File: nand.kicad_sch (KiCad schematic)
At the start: 20 parts, among them U6 IS21ES08GA-JQLI-TR

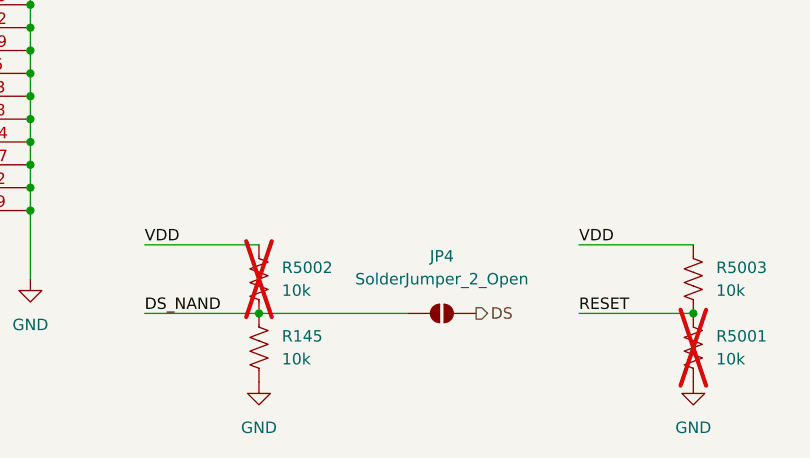
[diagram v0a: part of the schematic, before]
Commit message: eMMC routing
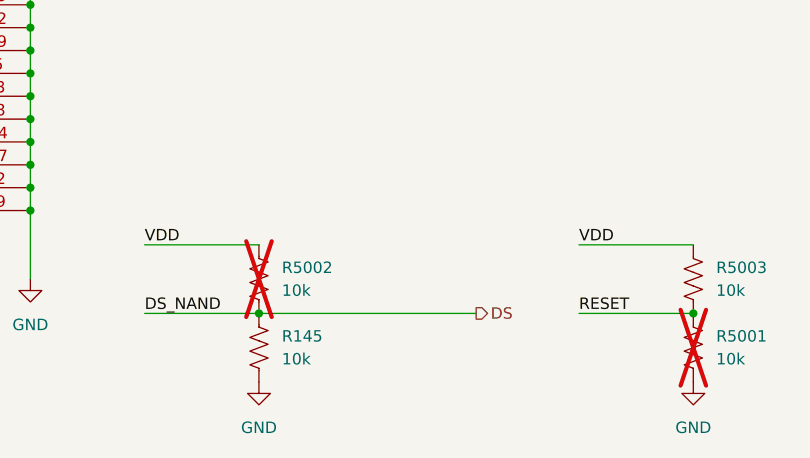
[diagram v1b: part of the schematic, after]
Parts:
- removed JP4: SolderJumper_2_Open, Jumper:SolderJumper-2_P1.3mm_Open_Pad1.0x1.5mm, symbol Jumper:SolderJumper_2_Open
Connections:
- net DS_NAND is gone; now on net DS: R145.1, R5002.2, U6.K5 (DS)
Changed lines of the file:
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@@
 	(wire
 		(pts
-			(xy 109.22 176.53) (xy 125.73 176.53)
+			(xy 109.22 176.53) (xy 133.35 176.53)
 		)
 		(stroke
@@
 					(unit 1)
 				)
-			)
-		)
-	)
-	(symbol
-		(lib_name "SolderJumper_2_Open_1")
-		(lib_id "Jumper:SolderJumper_2_Open")
-		(at 129.54 176.53 0)
-		(unit 1)
-		(exclude_from_sim no)
-		(in_bom no)
-		(on_board yes)
-		(dnp no)
-		(fields_autoplaced yes)
-		(property "Reference" "JP4"
-			(at 129.54 170.18 0)
-			(effects
-				(font
-					(size 1.27 1.27)
-				)
-			)
-		)
-		(property "Value" "SolderJumper_2_Open"
-			(at 129.54 172.72 0)
-			(effects
-				(font
-					(size 1.27 1.27)
-				)
-			)
-		)
-		(property "Footprint" "Jumper:SolderJumper-2_P1.3mm_Open_Pad1.0x1.5mm"
-			(at 129.54 176.53 0)
-			(effects
-				(font
-					(size 1.27 1.27)
-				)
-				(hide yes)
-			)
-		)
-		(property "Datasheet" "~"
-			(at 129.54 176.53 0)
-			(effects
-				(font
-					(size 1.27 1.27)
-				)
-				(hide yes)
-			)
-		)
-		(property "Description" "Solder Jumper, 2-pole, open"
-			(at 129.54 176.53 0)
-			(effects
-				(font
-					(size 1.27 1.27)
-				)
-				(hide yes)
-			)
-		)
-		(pin "2"
-		)
-		(pin "1"
-		)
-		(instances
-			(project ""
-				(path "/21bb932a-ec67-4661-9215-0551f718d1c0/dbc4538f-6782-4334-8773-c54462e4bd8b"
-					(reference "JP4")
-					(unit 1)
-				)

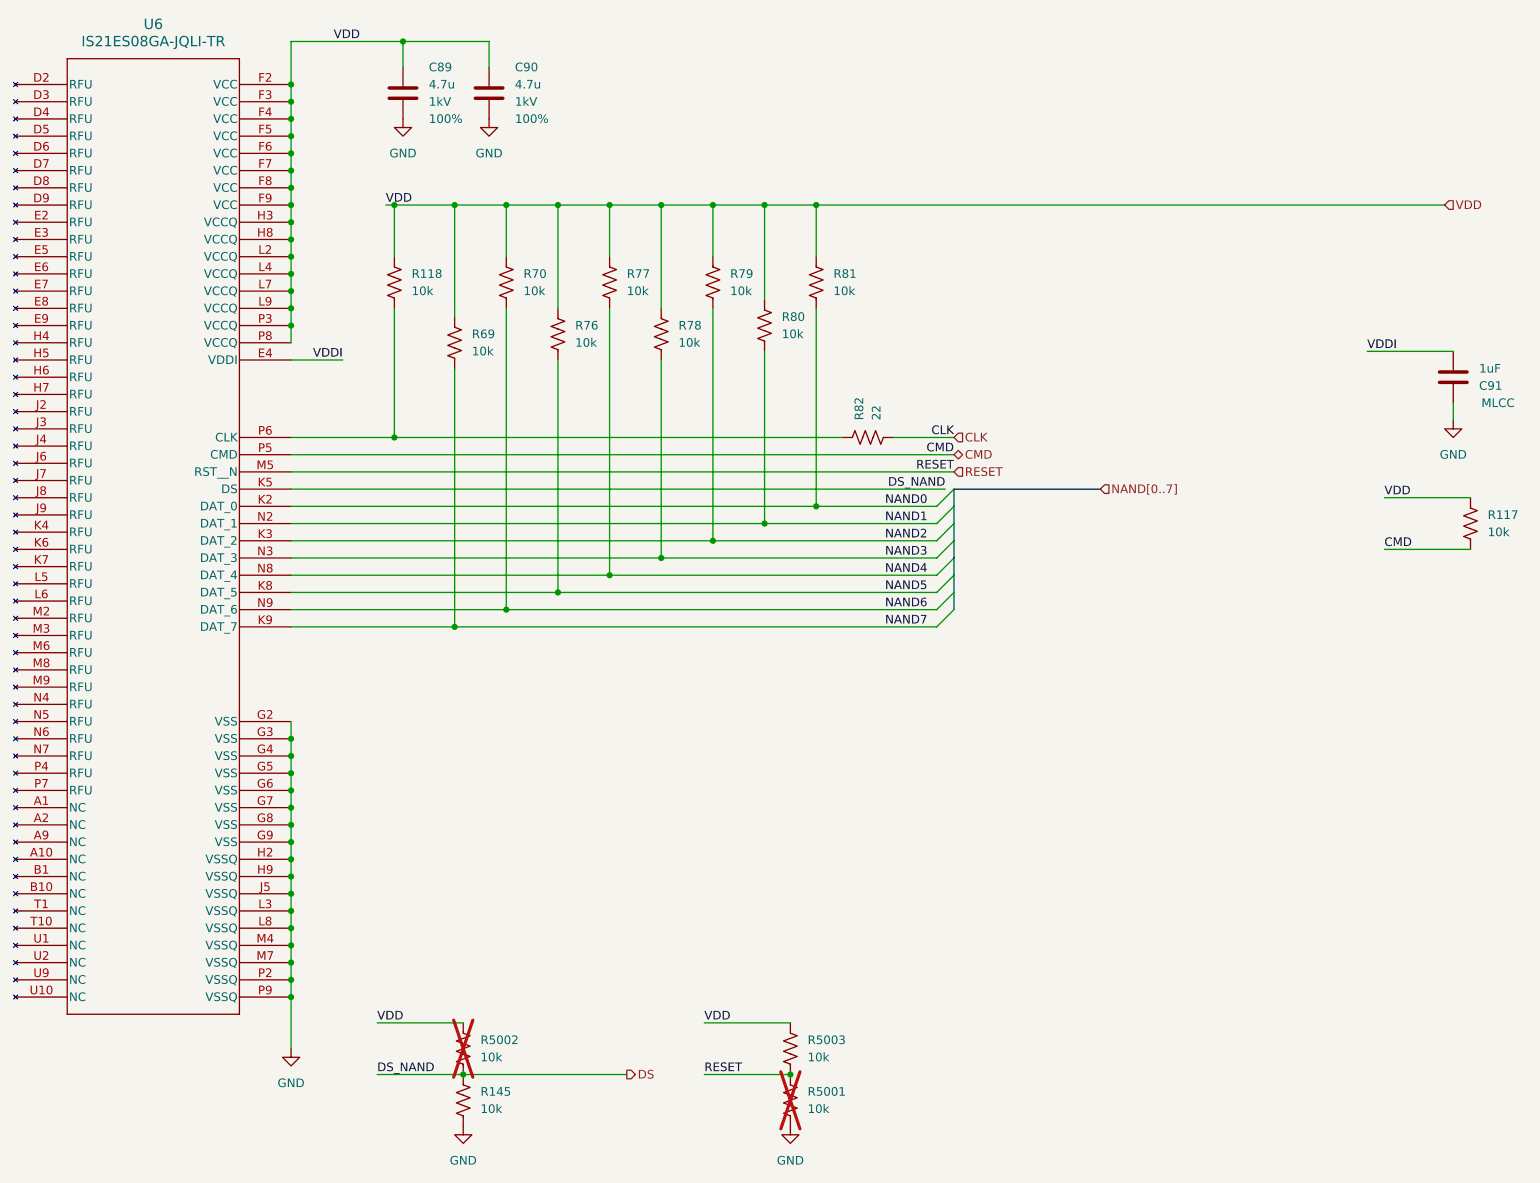
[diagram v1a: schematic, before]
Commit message: Organizing REFDES
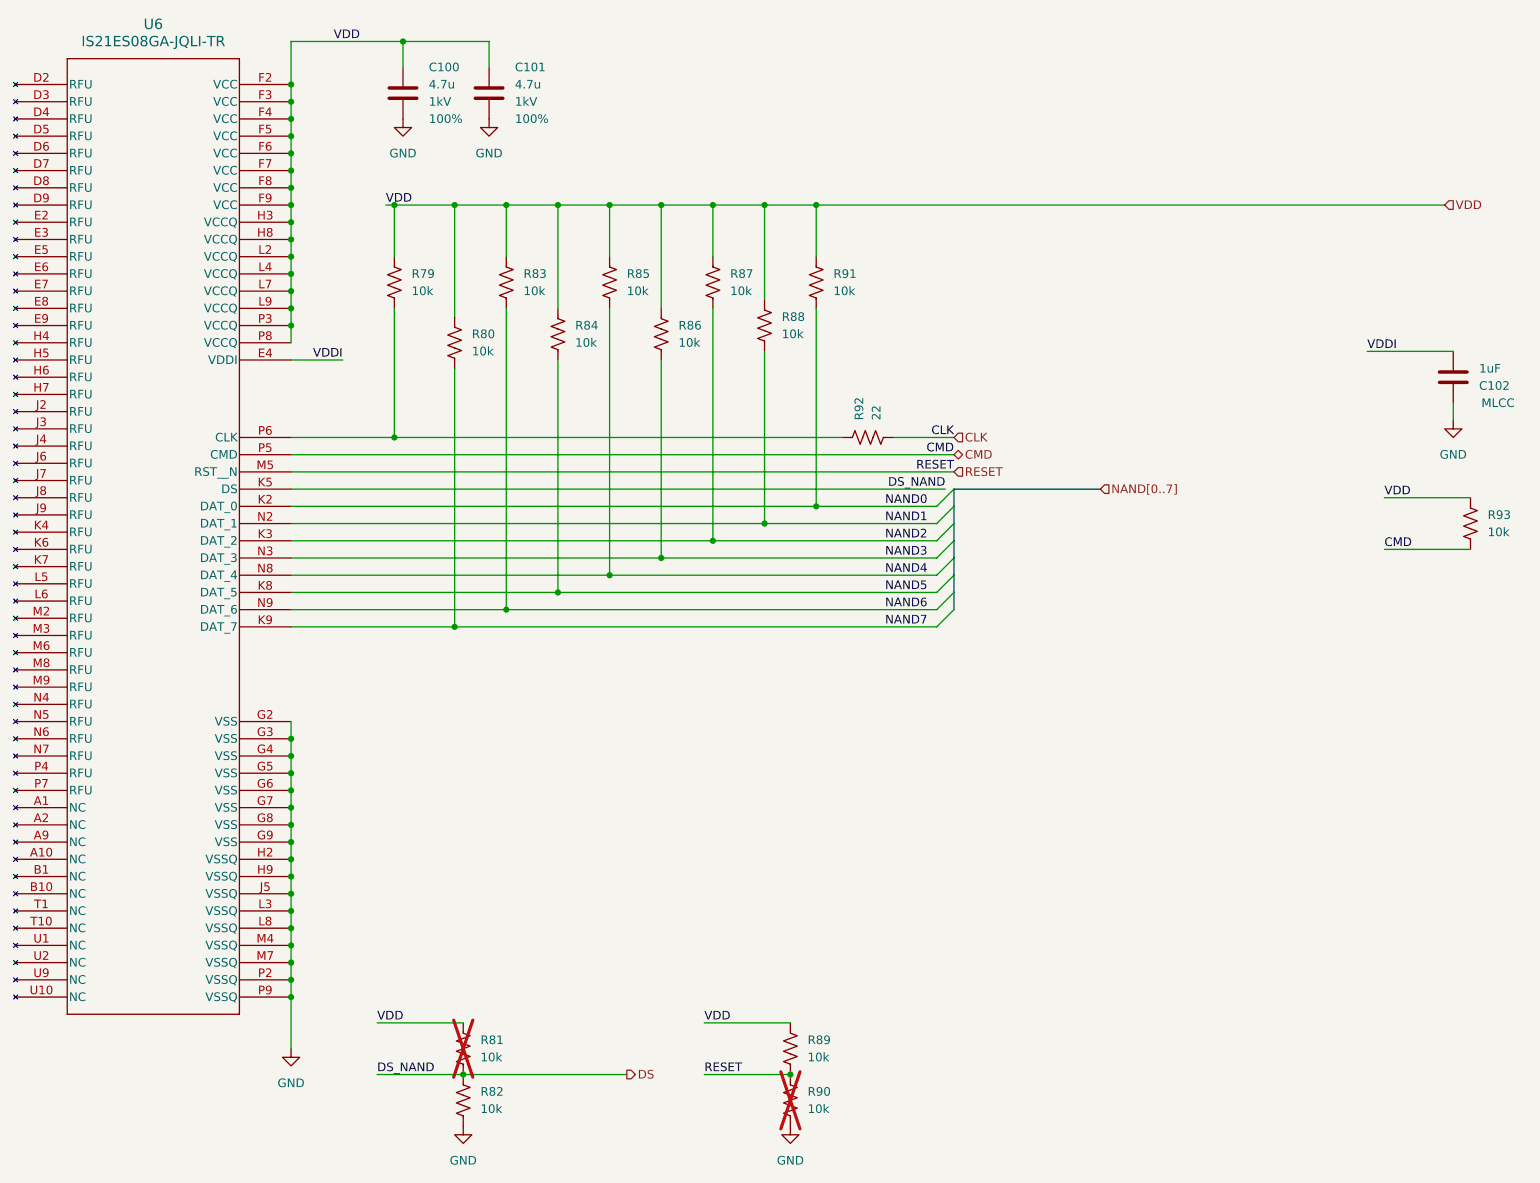
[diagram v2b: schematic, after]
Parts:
- renumbered C89 to C100, C90 to C101, C91 to C102, R118 to R79, R69 to R80, R5002 to R81, R145 to R82, R70 to R83, R76 to R84, R77 to R85, R78 to R86, R79 to R87, R80 to R88, R5003 to R89, R5001 to R90, R81 to R91, R82 to R92, R117 to R93
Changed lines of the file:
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@@
 		(dnp no)
 		(fields_autoplaced yes)
-		(property "Reference" "#PWR0218"
+		(property "Reference" "#PWR0173"
 			(at 255.27 86.36 0)
 			(effects
@@
 			(project "SBC"
 				(path "/21bb932a-ec67-4661-9215-0551f718d1c0/dbc4538f-6782-4334-8773-c54462e4bd8b"
-					(reference "#PWR0218")
+					(reference "#PWR0173")
 					(unit 1)
 				)
@@
 		(dnp no)
 		(fields_autoplaced yes)
-		(property "Reference" "#PWR0253"
+		(property "Reference" "#PWR0169"
 			(at 100.33 41.91 0)
 			(effects
@@
 			(project "SBC"
 				(path "/21bb932a-ec67-4661-9215-0551f718d1c0/dbc4538f-6782-4334-8773-c54462e4bd8b"
-					(reference "#PWR0253")
+					(reference "#PWR0169")
 					(unit 1)
 				)
@@
 		(dnp no)
 		(fields_autoplaced yes)
-		(property "Reference" "C89"
+		(property "Reference" "C100"
 			(at 104.14 27.9399 0)
 			(effects
@@
 			(project "SBC"
 				(path "/21bb932a-ec67-4661-9215-0551f718d1c0/dbc4538f-6782-4334-8773-c54462e4bd8b"
-					(reference "C89")
+					(reference "C100")
 					(unit 1)
 				)
@@
 		(on_board yes)
 		(dnp no)
-		(property "Reference" "R118"
+		(property "Reference" "R79"
 			(at 101.6 58.4199 90)
 			(effects
@@
 			(project "SBC"
 				(path "/21bb932a-ec67-4661-9215-0551f718d1c0/dbc4538f-6782-4334-8773-c54462e4bd8b"
-					(reference "R118")
+					(reference "R79")
 					(unit 1)
 				)
@@
 		(on_board yes)
 		(dnp no)
-		(property "Reference" "R69"
+		(property "Reference" "R80"
 			(at 110.49 67.3099 90)
 			(effects
@@
 			(project "SBC"
 				(path "/21bb932a-ec67-4661-9215-0551f718d1c0/dbc4538f-6782-4334-8773-c54462e4bd8b"
-					(reference "R69")
+					(reference "R80")
 					(unit 1)
 				)
@@
 		(dnp no)
 		(fields_autoplaced yes)
-		(property "Reference" "C90"
+		(property "Reference" "C101"
 			(at 116.84 27.9399 0)
 			(effects
@@
 			(project "SBC"
 				(path "/21bb932a-ec67-4661-9215-0551f718d1c0/dbc4538f-6782-4334-8773-c54462e4bd8b"
-					(reference "C90")
+					(reference "C101")
 					(unit 1)
 				)
@@
 		(on_board yes)
 		(dnp no)
-		(property "Reference" "R5003"
+		(property "Reference" "R89"
 			(at 160.02 171.4499 90)
 			(effects
@@
 			(project "SBC"
 				(path "/21bb932a-ec67-4661-9215-0551f718d1c0/dbc4538f-6782-4334-8773-c54462e4bd8b"
-					(reference "R5003")
+					(reference "R89")
 					(unit 1)
 				)
@@
 		(dnp no)
 		(fields_autoplaced yes)
-		(property "Reference" "#PWR05001"
+		(property "Reference" "#PWR0172"
 			(at 157.48 190.5 0)
 			(effects
@@
 			(project "SBC"
 				(path "/21bb932a-ec67-4661-9215-0551f718d1c0/dbc4538f-6782-4334-8773-c54462e4bd8b"
-					(reference "#PWR05001")
+					(reference "#PWR0172")
 					(unit 1)
 				)
@@
 		(on_board yes)
 		(dnp no)
-		(property "Reference" "R81"
+		(property "Reference" "R91"
 			(at 163.83 58.4199 90)
 			(effects
@@
 			(project "SBC"
 				(path "/21bb932a-ec67-4661-9215-0551f718d1c0/dbc4538f-6782-4334-8773-c54462e4bd8b"
-					(reference "R81")
+					(reference "R91")
 					(unit 1)
 				)
@@
 		(on_board yes)
 		(dnp yes)
-		(property "Reference" "R5002"
+		(property "Reference" "R81"
 			(at 111.76 171.4499 90)
 			(effects
@@
 			(project "SBC"
 				(path "/21bb932a-ec67-4661-9215-0551f718d1c0/dbc4538f-6782-4334-8773-c54462e4bd8b"
-					(reference "R5002")
+					(reference "R81")
 					(unit 1)
 				)
@@
 		(on_board yes)
 		(dnp no)
-		(property "Reference" "R77"
+		(property "Reference" "R85"
 			(at 133.35 58.4199 90)
 			(effects
@@
 			(project "SBC"
 				(path "/21bb932a-ec67-4661-9215-0551f718d1c0/dbc4538f-6782-4334-8773-c54462e4bd8b"
-					(reference "R77")
+					(reference "R85")
 					(unit 1)
 				)
@@
 		(on_board yes)
 		(dnp no)
-		(property "Reference" "R76"
+		(property "Reference" "R84"
 			(at 125.73 66.0399 90)
 			(effects
@@
 			(project "SBC"
 				(path "/21bb932a-ec67-4661-9215-0551f718d1c0/dbc4538f-6782-4334-8773-c54462e4bd8b"
-					(reference "R76")
+					(reference "R84")
 					(unit 1)
 				)
@@
 		(on_board yes)
 		(dnp no)
-		(property "Reference" "R117"
+		(property "Reference" "R93"
 			(at 260.35 93.9799 90)
 			(effects
@@
 			(project "SBC"
 				(path "/21bb932a-ec67-4661-9215-0551f718d1c0/dbc4538f-6782-4334-8773-c54462e4bd8b"
-					(reference "R117")
+					(reference "R93")
 					(unit 1)
 				)
@@
 		(on_board yes)
 		(dnp no)
-		(property "Reference" "R145"
+		(property "Reference" "R82"
 			(at 111.76 179.0699 90)
 			(effects
@@
 			(project "SBC"
 				(path "/21bb932a-ec67-4661-9215-0551f718d1c0/dbc4538f-6782-4334-8773-c54462e4bd8b"
-					(reference "R145")
+					(reference "R82")
 					(unit 1)
 				)
@@
 		(on_board yes)
 		(dnp no)
-		(property "Reference" "R82"
+		(property "Reference" "R92"
 			(at 167.6399 80.01 90)
 			(effects
@@
 			(project "SBC"
 				(path "/21bb932a-ec67-4661-9215-0551f718d1c0/dbc4538f-6782-4334-8773-c54462e4bd8b"
-					(reference "R82")
+					(reference "R92")
 					(unit 1)
 				)
@@
 		(on_board yes)
 		(dnp no)
-		(property "Reference" "R78"
+		(property "Reference" "R86"
 			(at 140.97 66.0399 90)
 			(effects
@@
 			(project "SBC"
 				(path "/21bb932a-ec67-4661-9215-0551f718d1c0/dbc4538f-6782-4334-8773-c54462e4bd8b"
-					(reference "R78")
+					(reference "R86")
 					(unit 1)
 				)
@@
 		(on_board yes)
 		(dnp no)
-		(property "Reference" "C91"
+		(property "Reference" "C102"
 			(at 259.08 74.93 0)
 			(effects
@@
 			(project "SBC"
 				(path "/21bb932a-ec67-4661-9215-0551f718d1c0/dbc4538f-6782-4334-8773-c54462e4bd8b"
-					(reference "C91")
+					(reference "C102")
 					(unit 1)
 				)
@@
 		(on_board yes)
 		(dnp yes)
-		(property "Reference" "R5001"
+		(property "Reference" "R90"
 			(at 160.02 179.0699 90)
 			(effects
@@
 			(project "SBC"
 				(path "/21bb932a-ec67-4661-9215-0551f718d1c0/dbc4538f-6782-4334-8773-c54462e4bd8b"
-					(reference "R5001")
+					(reference "R90")
 					(unit 1)
 				)
@@
 		(dnp no)
 		(fields_autoplaced yes)
-		(property "Reference" "#PWR0219"
+		(property "Reference" "#PWR0168"
 			(at 83.82 179.07 0)
 			(effects
@@
 			(project ""
 				(path "/21bb932a-ec67-4661-9215-0551f718d1c0/dbc4538f-6782-4334-8773-c54462e4bd8b"
-					(reference "#PWR0219")
+					(reference "#PWR0168")
 					(unit 1)
 				)
@@
 		(on_board yes)
 		(dnp no)
-		(property "Reference" "R79"
+		(property "Reference" "R87"
 			(at 148.59 58.4199 90)
 			(effects
@@
 			(project "SBC"
 				(path "/21bb932a-ec67-4661-9215-0551f718d1c0/dbc4538f-6782-4334-8773-c54462e4bd8b"
-					(reference "R79")
+					(reference "R87")
 					(unit 1)
 				)
@@
 		(dnp no)
 		(fields_autoplaced yes)
-		(property "Reference" "#PWR0254"
+		(property "Reference" "#PWR0171"
 			(at 113.03 41.91 0)
 			(effects
@@
 			(project "SBC"
 				(path "/21bb932a-ec67-4661-9215-0551f718d1c0/dbc4538f-6782-4334-8773-c54462e4bd8b"
-					(reference "#PWR0254")
+					(reference "#PWR0171")
 					(unit 1)
 				)
@@
 		(on_board yes)
 		(dnp no)
-		(property "Reference" "R80"
+		(property "Reference" "R88"
 			(at 156.21 64.7699 90)
 			(effects
@@
 			(project "SBC"
 				(path "/21bb932a-ec67-4661-9215-0551f718d1c0/dbc4538f-6782-4334-8773-c54462e4bd8b"
-					(reference "R80")
+					(reference "R88")
 					(unit 1)
 				)
@@
 		(on_board yes)
 		(dnp no)
-		(property "Reference" "R70"
+		(property "Reference" "R83"
 			(at 118.11 58.4199 90)
 			(effects
@@
 			(project "SBC"
 				(path "/21bb932a-ec67-4661-9215-0551f718d1c0/dbc4538f-6782-4334-8773-c54462e4bd8b"
-					(reference "R70")
+					(reference "R83")
 					(unit 1)
 				)
@@
 		(dnp no)
 		(fields_autoplaced yes)
-		(property "Reference" "#PWR0255"
+		(property "Reference" "#PWR0170"
 			(at 109.22 190.5 0)
 			(effects
@@
 			(project "SBC"
 				(path "/21bb932a-ec67-4661-9215-0551f718d1c0/dbc4538f-6782-4334-8773-c54462e4bd8b"
-					(reference "#PWR0255")
-					(unit 1)
-				)
+					(reference "#PWR0170")
+					(unit 1)
+				)
